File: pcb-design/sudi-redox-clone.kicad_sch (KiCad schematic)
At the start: 127 parts, among them J1 SIDE_CON, J2 0.91 OLED, J3 SWD_JLINK, J5 SIDE_CON, J8 BatCon, K1 KEYSW, K10 KEYSW, K11 KEYSW, K12 KEYSW, K13 KEYSW, K14 KEYSW, K15 KEYSW, K16 KEYSW, K17 KEYSW, K18 KEYSW, K2 KEYSW, K3 KEYSW, K4 KEYSW, K5 KEYSW, K6 KEYSW, K7 KEYSW, K8 KEYSW, K9 KEYSW, P1 USB_C_Plug_USB2.0, SW1 RST, U4 AMS1117-3.3, U5 CH340C, U6 TP4056, U7 nRF52832-QFxx, U8 MCP23017_SS, Y5 32MHz

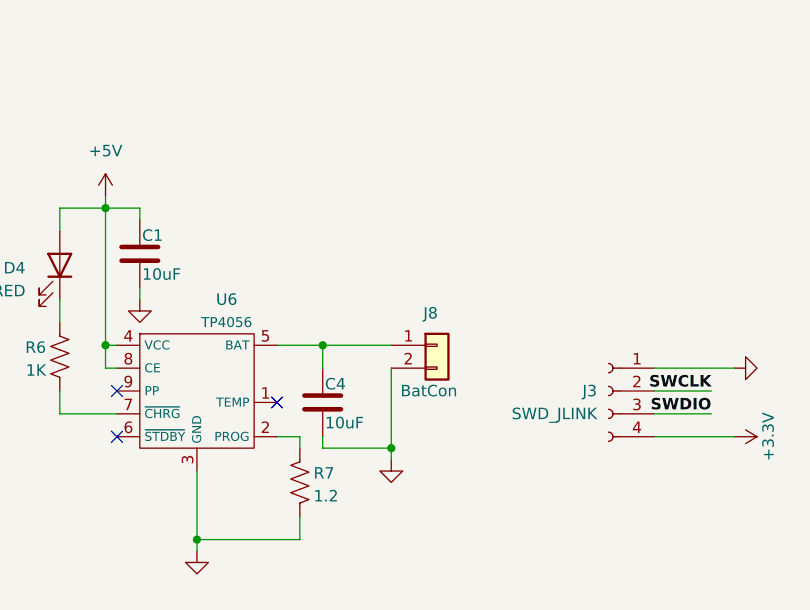
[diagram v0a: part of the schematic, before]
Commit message: [11-13-0459] add svg and switch to schematic
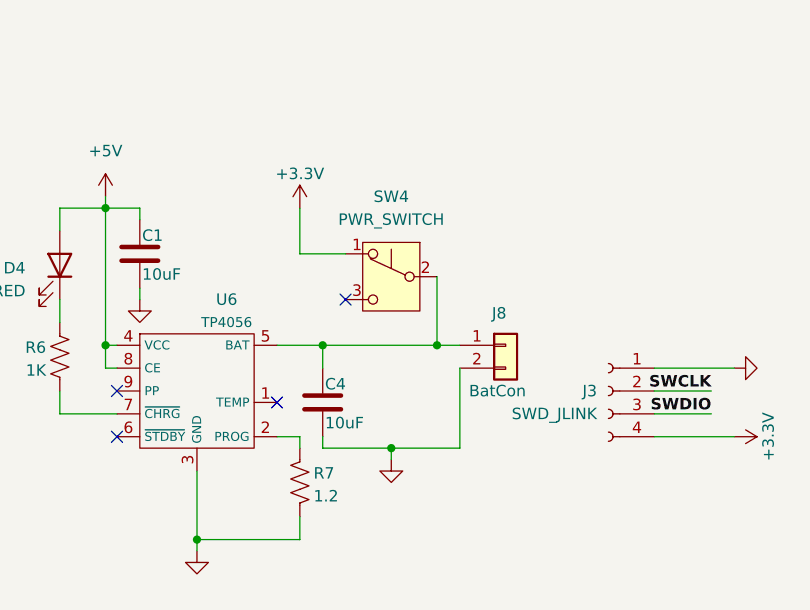
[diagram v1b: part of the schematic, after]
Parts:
- added SW4: PWR_SWITCH, Button_Switch_SMD:SW_SPDT_CK_JS102011SAQN, symbol Switch:SW_Push_SPDT
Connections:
- net +3.3V: now also SW4.1 (A)
- net at C4.1, J8.1 (Pin_1), U6.5 (BAT): now also SW4.2 (B)
- no-connect marks 28 -> 29
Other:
- moved on the sheet: J8
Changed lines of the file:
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@@
 	)
 	(junction
+		(at 177.8 49.53)
+		(diameter 0)
+		(color 0 0 0 0)
+	)
+	(junction
 		(at 330.2 182.88)
 		(diameter 0)
@@
 	)
 	(no_connect
+		(at 167.64 44.45)
+	)
+	(no_connect
 		(at 88.9 85.09)
 	)
@@
 	(wire
 		(pts
+			(xy 180.34 60.96) (xy 172.72 60.96)
+		)
+		(stroke
+			(width 0)
+			(type default)
+		)
+	)
+	(wire
+		(pts
 			(xy 247.65 101.6) (xy 250.19 101.6)
 		)
@@
 	(wire
 		(pts
-			(xy 172.72 52.07) (xy 172.72 60.96)
+			(xy 180.34 52.07) (xy 180.34 60.96)
 		)
 		(stroke
@@
 	(wire
 		(pts
+			(xy 167.64 39.37) (xy 162.56 39.37)
+		)
+		(stroke
+			(width 0)
+			(type default)
+		)
+	)
+	(wire
+		(pts
 			(xy 62.23 48.26) (xy 62.23 49.53)
 		)
@@
 	(wire
 		(pts
+			(xy 177.8 49.53) (xy 180.34 49.53)
+		)
+		(stroke
+			(width 0)
+			(type default)
+		)
+	)
+	(wire
+		(pts
 			(xy 228.6 161.29) (xy 231.14 161.29)
 		)
@@
 	(wire
 		(pts
-			(xy 165.1 49.53) (xy 172.72 49.53)
+			(xy 165.1 49.53) (xy 177.8 49.53)
 		)
 		(stroke
@@
 	(wire
 		(pts
+			(xy 162.56 39.37) (xy 162.56 34.29)
+		)
+		(stroke
+			(width 0)
+			(type default)
+		)
+	)
+	(wire
+		(pts
 			(xy 191.77 201.93) (xy 193.04 201.93)
 		)
@@
 	(wire
 		(pts
+			(xy 177.8 41.91) (xy 177.8 49.53)
+		)
+		(stroke
+			(width 0)
+			(type default)
+		)
+	)
+	(wire
+		(pts
 			(xy 278.13 26.67) (xy 278.13 30.48)
 		)
@@
 	)
 	(symbol
+		(lib_id "power:+3.3V")
+		(at 162.56 34.29 0)
+		(unit 1)
+		(exclude_from_sim no)
+		(in_bom yes)
+		(on_board yes)
+		(dnp no)
+		(fields_autoplaced yes)
+		(property "Reference" "#PWR035"
+			(at 162.56 38.1 0)
+			(effects
+				(font
+					(size 1.27 1.27)
+				)
+				(hide yes)
+			)
+		)
+		(property "Value" "+3.3V"
+			(at 162.56 30.48 0)
+			(effects
+				(font
+					(size 1.27 1.27)
+				)
+			)
+		)
+		(property "Footprint" ""
+			(at 162.56 34.29 0)
+			(effects
+				(font
+					(size 1.27 1.27)
+				)
+				(hide yes)
+			)
+		)
+		(property "Datasheet" ""
+			(at 162.56 34.29 0)
+			(effects
+				(font
+					(size 1.27 1.27)
+				)
+				(hide yes)
+			)
+		)
+		(property "Description" "Power symbol creates a global label with name \"+3.3V\""
+			(at 162.56 34.29 0)
+			(effects
+				(font
+					(size 1.27 1.27)
+				)
+				(hide yes)
+			)
+		)
+		(pin "1"
+		)
+		(instances
+			(project "sudi-redox-clone"
+				(path "/5bbd2338-13ff-49b0-9f87-5cbfec528c5b"
+					(reference "#PWR035")
+					(unit 1)
+				)
+			)
+		)
+	)
+	(symbol
 		(lib_id "Connector:TestPoint")
 		(at 119.38 152.4 270)
@@
 	(symbol
 		(lib_id "Connector_Generic:Conn_01x02")
-		(at 177.8 49.53 0)
+		(at 185.42 49.53 0)
 		(unit 1)
 		(exclude_from_sim no)
@@
 		(dnp no)
 		(property "Reference" "J8"
-			(at 176.276 45.974 0)
+			(at 183.896 45.974 0)
 			(effects
 				(font
@@
 		)
 		(property "Value" "BatCon"
-			(at 173.736 54.61 0)
+			(at 181.356 54.61 0)
 			(effects
 				(font
@@
 		)
 		(property "Footprint" "Connector_PinHeader_2.54mm:PinHeader_1x02_P2.54mm_Horizontal"
-			(at 177.8 49.53 0)
+			(at 185.42 49.53 0)
 			(effects
 				(font
@@
 		)
 		(property "Datasheet" "~"
-			(at 177.8 49.53 0)
+			(at 185.42 49.53 0)
 			(effects
 				(font
@@
 		)
 		(property "Description" "Generic connector, single row, 01x02, script generated (kicad-library-utils/schlib/autogen/connector/)"
-			(at 177.8 49.53 0)
+			(at 185.42 49.53 0)
 			(effects
 				(font
@@
 					(unit 1)
 				)
+			)
+		)
+	)
+	(symbol
+		(lib_id "Switch:SW_Push_SPDT")
+		(at 172.72 41.91 0)
+		(mirror y)
+		(unit 1)
+		(exclude_from_sim no)
+		(in_bom yes)
+		(on_board yes)
+		(dnp no)
+		(property "Reference" "SW4"
+			(at 172.72 33.02 0)
+			(effects
+				(font
+					(size 1.27 1.27)
+				)
+			)
+		)
+		(property "Value" "PWR_SWITCH"
+			(at 172.72 35.56 0)
+			(effects
+				(font
+					(size 1.27 1.27)
+				)
+			)
+		)
+		(property "Footprint" "Button_Switch_SMD:SW_SPDT_CK_JS102011SAQN"
+			(at 172.72 41.91 0)
+			(effects
+				(font
+					(size 1.27 1.27)
+				)
+				(hide yes)
+			)
+		)
+		(property "Datasheet" "~"
+			(at 172.72 41.91 0)
+			(effects
+				(font
+					(size 1.27 1.27)
+				)
+				(hide yes)
+			)
+		)
+		(property "Description" "Momentary Switch, single pole double throw"
+			(at 172.72 41.91 0)
+			(effects
+				(font
+					(size 1.27 1.27)
+				)
+				(hide yes)
+			)
+		)
+		(pin "3"
+		)
+		(pin "2"
+		)
+		(pin "1"
+		)
+		(instances
+			(project "sudi-redox-clone"
+				(path "/5bbd2338-13ff-49b0-9f87-5cbfec528c5b"
+					(reference "SW4")
+					(unit 1)
+				)

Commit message: [14-11-2129] init SUDI development board
nit
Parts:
- added U10: nRF52820-QDxx, Package_DFN_QFN:QFN-40-1EP_5x5mm_P0.4mm_EP3.6x3.6mm, symbol MCU_Nordic:nRF52820-QDxx
- added U9: nRF52833_QDxx, Package_DFN_QFN:QFN-40-1EP_5x5mm_P0.4mm_EP3.6x3.6mm, symbol MCU_Nordic:nRF52833_QDxx
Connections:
- new net: U10.37 (VSS), U10.41 (VSS)
- new net: U9.18 (VDD), U9.30 (VDD), U9.40 (VDD), U9.8 (VDD)
- new net: U9.37 (VSS), U9.41 (VSS)

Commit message: [16-11-1807] change chargin mechanism
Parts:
- removed AE3: 2.4GHz, RF_Antenna:Texas_SWRA117D_2.4GHz_Left, symbol Device:Antenna
- removed C3: 10uF/5V, Capacitor_SMD:C_0805_2012Metric_Pad1.18x1.45mm_HandSolder, symbol Device:C_Polarized
- removed C41: 0.8pF, Capacitor_SMD:C_0805_2012Metric_Pad1.18x1.45mm_HandSolder, symbol Device:C
- removed C42: 100nF, Capacitor_SMD:C_0805_2012Metric_Pad1.18x1.45mm_HandSolder, symbol Device:C
- removed D10, D11, D12, D16, D17, D18, D22, D23, D24, D28, D43, D44, D45, D46, D47, D48, D5, D6: WS2812B, CustomWS2185BFootPrint:LED_WS2812B_PLCC4_5.0x5.0mm_P3.2mm, symbol LED:WS2812B
- removed D13, D19, D25, D29, D30, D31, D8, D9: 1N5820, canadian_footprints:D_SOD123_axial-dual, symbol Diode:1N5820
- removed H8, H9: MountingHole_Pad, MountingHole:MountingHole_3.2mm_M3_DIN965_Pad, symbol Mechanical:MountingHole_Pad
- removed J8: BatCon, Connector_PinHeader_2.54mm:PinHeader_1x02_P2.54mm_Horizontal, symbol Connector_Generic:Conn_01x02
- removed L7: 3.9nH, Inductor_SMD:L_0603_1608Metric_Pad1.05x0.95mm_HandSolder, symbol Device:L
- removed U10: nRF52820-QDxx, Package_DFN_QFN:QFN-40-1EP_5x5mm_P0.4mm_EP3.6x3.6mm, symbol MCU_Nordic:nRF52820-QDxx
- removed U4: AMS1117-3.3, Package_TO_SOT_SMD:SOT-223-3_TabPin2, symbol Regulator_Linear:AMS1117-3.3
- removed U5: CH340C, Package_SO:SOIC-16_3.9x9.9mm_P1.27mm, symbol Interface_USB:CH340C
- removed U6: TP4056, Package_SO:SOIC-8-1EP_3.9x4.9mm_P1.27mm_EP2.29x3mm, symbol tp4056:TP4056
- removed U9: nRF52833_QDxx, Package_DFN_QFN:QFN-40-1EP_5x5mm_P0.4mm_EP3.6x3.6mm, symbol MCU_Nordic:nRF52833_QDxx
- removed Y5: 32MHz, Crystal:Crystal_SMD_2016-4Pin_2.0x1.6mm, symbol Device:Crystal_GND24
- added AE1: 2.4GHz, RF_Antenna:Texas_SWRA117D_2.4GHz_Left, symbol Device:Antenna
- added C11, C15: 0.1uF, Capacitor_SMD:C_0805_2012Metric_Pad1.18x1.45mm_HandSolder, symbol Device:C
- added C12, C13, C14, C16, C17: 10uF, Capacitor_SMD:C_0805_2012Metric_Pad1.18x1.45mm_HandSolder, symbol Device:C
- added C18: 12pF, Capacitor_SMD:C_0805_2012Metric_Pad1.18x1.45mm_HandSolder, symbol Device:C
- added C21: 0.8pF, Capacitor_SMD:C_0805_2012Metric_Pad1.18x1.45mm_HandSolder, symbol Device:C
- added C3: 4.7uF, Capacitor_SMD:C_0805_2012Metric_Pad1.18x1.45mm_HandSolder, symbol Device:C
- added D10, D11, D12, D13, D17, D18, D19, D23, D24, D25, D29, D30, D31, D36, D37, D38, D8, D9: WS2812B, LED_SMD:LED_WS2812B-2020_PLCC4_2.0x2.0mm, symbol LED:WS2812B-2020
- added D16, D22, D28, D33, D34, D35, D5, D6: 1N4148, canadian_footprints:D_SOD123_axial-dual, symbol Diode:1N5820
- added D32: red, LED_SMD:LED_0805_2012Metric_Pad1.15x1.40mm_HandSolder, symbol Device:LED
- added H1, H2: MountingHole_Pad, MountingHole:MountingHole_3.2mm_M3_DIN965_Pad, symbol Mechanical:MountingHole_Pad
- added J4: BatCon, Connector_PinHeader_2.54mm:PinHeader_1x02_P2.54mm_Horizontal, symbol Connector_Generic:Conn_01x02
- added JP1: END_TX, Jumper:SolderJumper-2_P1.3mm_Open_RoundedPad1.0x1.5mm, symbol Jumper:SolderJumper_2_Open
- added L1, L2: 22uH, Inductor_SMD:L_0603_1608Metric_Pad1.05x0.95mm_HandSolder, symbol Device:L
- added L3: 3.9nH, Inductor_SMD:L_0603_1608Metric_Pad1.05x0.95mm_HandSolder, symbol Device:L
- added Q1: PJA3404_(G1,D3,S2), Package_TO_SOT_SMD:SOT-23, symbol Simulation_SPICE:NMOS
- added Q2: PJA3405_(G1,D3,S2), Package_TO_SOT_SMD:SOT-23, symbol Simulation_SPICE:PMOS
- added R11: 1k, Resistor_SMD:R_0805_2012Metric_Pad1.20x1.40mm_HandSolder, symbol Device:R_US
- added R12, R5: 100k, Resistor_SMD:R_0805_2012Metric_Pad1.20x1.40mm_HandSolder, symbol Device:R_US
- added R13, R16: 100, Resistor_SMD:R_0805_2012Metric_Pad1.20x1.40mm_HandSolder, symbol Device:R_US
- added R14: 1.13k, Resistor_SMD:R_0805_2012Metric_Pad1.20x1.40mm_HandSolder, symbol Device:R_US
- added R15, R17: 1K, Resistor_SMD:R_0805_2012Metric_Pad1.20x1.40mm_HandSolder, symbol Device:R_US
- added SW3: PWR_SWITCH, Button_Switch_SMD:SW_SPDT_PCM12, symbol Switch:SW_Push_SPDT
- added U4: CH340C, Package_SO:SOIC-16_3.9x9.9mm_P1.27mm, symbol Interface_USB:CH340C
- added U5: BQ24075RGT_DPPM, Package_DFN_QFN:VQFN-16-1EP_3x3mm_P0.5mm_EP1.6x1.6mm, symbol Battery_Management:BQ24075RGT
- added U6: TPS63002_SEPIC_5V, Package_SON:Texas_DRC0010J_ThermalVias, symbol Regulator_Switching:TPS63002
- added U9: TPS63001_SEPIC_3V3, Package_SON:Texas_DRC0010J_ThermalVias, symbol Regulator_Switching:TPS63001
- added Y1: 32MHz_CF4032M00020001, Crystal:Crystal_SMD_2016-4Pin_2.0x1.6mm, symbol Device:Crystal_GND24
- C1: value 10uF -> 4.7uF
- C19: value 12pF -> 100nF
- C36: value 100nF -> 100nF/NC
- C40: value 100nF/NC -> 100nF
- D1, D14, D15, D2, D20, D21, D26, D27, D3, D7: value 1N5820 -> 1N4148
- D4: value RED -> green
- J2: value 0.91 OLED -> SWD_JLINK; footprint Connector_PinHeader_2.54mm:PinHeader_1x04_P2.54mm_Vertical -> Connector_PinHeader_2.54mm:PinHeader_1x04_P2.54mm_Horizontal
- J3: value SWD_JLINK -> 0.91 OLED; footprint Connector_PinHeader_2.54mm:PinHeader_1x04_P2.54mm_Horizontal -> Connector_PinHeader_2.54mm:PinHeader_1x04_P2.54mm_Vertical
- R6: value 1K -> 46.4K
- R7: value 1.2 -> 1.18k
- SW4: value PWR_SWITCH -> 5V_EN; footprint Button_Switch_SMD:SW_SPDT_CK_JS102011SAQN -> Button_Switch_SMD:SW_SPDT_PCM12
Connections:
- net +3.3V: now also C38.1, C39.1, C40.1, J1.B9 (CC1), J2.4 (Pin_4), J3.2 (Pin_2), J5.B9 (CC1), C16.1, C17.1, U4.16 (VCC), U4.4 (V3), U9.1 (VOUT), U9.10 (FB); no longer C20.1, C35.1, C36.1, J3.4 (Pin_4), SW4.1 (A)
- net +5V: now also C12.1, C13.1, D10.4 (VDD), D11.4 (VDD), D12.4 (VDD), D13.4 (VDD), D17.4 (VDD), D18.4 (VDD), D19.4 (VDD), D23.4 (VDD), D24.4 (VDD), D25.4 (VDD), D29.4 (VDD), D30.4 (VDD), D31.4 (VDD), D36.4 (VDD), D37.4 (VDD), D38.4 (VDD), D8.4 (VDD), D9.4 (VDD), U6.1 (VOUT), U6.10 (FB); no longer C1.1, C2.1, D4.2 (A), FB1.2
- net GND: now also C19.2, C20.1, C35.1, C36.1, C38.2, C39.2, C40.2, R6.2, R7.2, SW4.3 (C), C11.2, C12.2, C13.2, C14.2, C15.2, C16.2, C17.2, C18.1, C21.2, C3.2, D10.2 (VSS), D11.2 (VSS), D12.2 (VSS), D13.2 (VSS), D17.2 (VSS), D18.2 (VSS), D19.2 (VSS), D23.2 (VSS), D24.2 (VSS), D25.2 (VSS), D29.2 (VSS), D30.2 (VSS), D31.2 (VSS), D36.2 (VSS), D37.2 (VSS), D38.2 (VSS), D8.2 (VSS), D9.2 (VSS), J4.1 (Pin_1), Q1.2 (S), Q2.1 (G), R14.2, R5.2, SW3.3 (C), U4.1 (GND), U5.17 (VSS), U5.4 (~{CE}), U5.6 (EN1), U5.8 (VSS), U6.11 (PGND), U6.3 (PGND), U6.9 (GND), U9.11 (PGND), U9.3 (PGND), U9.9 (GND), Y1.2, Y1.4; no longer C19.1, C20.2, C35.2, C36.2, C38.1, C39.1, C40.1, R7.1
- net P0.00/XL1: now also TP1.1; no longer TP13.1
- net P0.01/XL2: now also TP2.1; no longer TP14.1
- net P0.02/AIN0: now also TP3.1; no longer TP15.1
- net P0.03/AIN1: now also TP4.1; no longer TP16.1
- net P0.04/AIN2: now also TP5.1; no longer TP17.1
- net P0.05/AIN3: now also TP6.1; no longer TP18.1
- net P0.19: now also TP7.1; no longer TP1.1
- net P0.20: now also TP8.1; no longer TP3.1
- net P0.22: now also TP9.1; no longer TP2.1
- net P0.23: now also TP10.1; no longer TP4.1
- net P0.24: now also TP11.1; no longer TP5.1
- net P0.25: now also TP12.1; no longer TP6.1
- net P0.26: now also TP13.1; no longer TP7.1
- net P0.27: now also TP14.1; no longer TP8.1
- net P0.28/AIN4: now also TP15.1; no longer TP9.1
- net P0.29/AIN5: now also TP16.1; no longer TP10.1
- net P0.30/AIN6: now also TP17.1; no longer TP11.1
- net P0.31/AIN7: now also TP18.1; no longer TP12.1
- net RX: now also U4.2 (TXD)
- net SCL: now also J3.3 (Pin_3); no longer J2.3 (Pin_3)
- net SDA: now also J3.4 (Pin_4); no longer J2.4 (Pin_4)
- net SWCLK: now also J2.2 (Pin_2); no longer J3.2 (Pin_2)
- net SWDIO: now also J2.3 (Pin_3); no longer J3.3 (Pin_3)
- net TX: now also D8.3 (DIN), JP1.2 (B), U4.3 (RXD)
- net row1: now also D14.1 (K), D20.1 (K), D26.1 (K), D33.1 (K), D5.1 (K); no longer D7.1 (K)
- net row2: now also D15.1 (K), D21.1 (K), D27.1 (K), D34.1 (K), D6.1 (K); no longer D14.1 (K), D20.1 (K), D26.1 (K)
- net row3: now also D7.1 (K), D16.1 (K), D22.1 (K), D28.1 (K), D35.1 (K); no longer D15.1 (K), D21.1 (K), D27.1 (K)
- net at K17.2: now also D34.2 (A)
- net at K13.2: now also D26.2 (A)
- net at K7.2: now also D14.2 (A)
- net at C8.2, U7.34 (XC1): now also Y1.3
- net at K6.2: now also D7.2 (A)
- net at K10.2: now also D20.2 (A)
- net at K4.2: now also D5.2 (A); no longer D7.2 (A)
- net at P1.A4 (VBUS), P1.A9 (VBUS), P1.B4 (VBUS)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: now also Q2.3 (D); no longer FB1.1
- net at P1.A6 (D+): now also U4.5 (UD+)
- net at P1.A7 (D-): now also U4.6 (UD-)
- net at K8.2: now also D15.2 (A); no longer D14.2 (A)
- net at K16.2: now also D33.2 (A)
- net at SW1.2, U7.24 (P0.21/~{RESET}): now also C19.1
- net at U7.33 (DEC3): now also C36.2; no longer C40.2
- net at U7.30 (ANT): now also C21.1, L3.2
- net at K11.2: now also D21.2 (A); no longer D20.2 (A)
- net at K15.2: now also D28.2 (A); no longer D27.2 (A)
- net at K14.2: now also D27.2 (A); no longer D26.2 (A)
- net at K12.2: now also D22.2 (A); no longer D21.2 (A)
- net at K9.2: now also D16.2 (A); no longer D15.2 (A)
- net at K5.2: now also D6.2 (A)
- net at U7.1 (DEC1): now also C20.2; no longer C38.2
- net at U7.32 (DEC2): now also C35.2; no longer C39.2
- net at U7.35 (XC2): now also C18.2, Y1.1; no longer C19.2
- net at K18.2: now also D35.2 (A)
- net at SW4.2 (B): now also U6.6 (EN); no longer C4.1
- net TMR: now reaches R6.1
- net TMR: now also U5.14 (TMR)
- net at D4.1 (K): now also U5.7 (~{PGOOD}); no longer R6.2
- removed net +3V7: J1.B9 (CC1), J2.2 (Pin_2), J5.B9 (CC1)
- net Tx renamed END_TX
- net END_TX: now also D38.1 (DOUT), JP1.1 (A)
- new net: D32.1 (K), U5.9 (~{CHG})
- new net: R12.2, SW3.1 (A)
- new net: AE1.1 (A), L3.1
- new net: D4.2 (A), R15.1
- new net: C15.1, R16.2, U9.6 (EN), U9.7 (PS/SYNC), U9.8 (VINA)
- new net: D13.1 (DOUT), D19.3 (DIN)
- new net: D10.1 (DOUT), D13.3 (DIN)
- new net: C11.1, R13.2, SW4.1 (A), U6.7 (PS/SYNC), U6.8 (VINA)
- new net: D30.1 (DOUT), D37.3 (DIN)
- new net: L2.1, U9.2 (L2)
- new net: L2.2, U9.4 (L1)
- new net: FB1.1, Q2.2 (S)
- new net: D25.1 (DOUT), D31.3 (DIN)
- new net: D19.1 (DOUT), D25.3 (DIN)
- new net: D12.1 (DOUT), D18.3 (DIN)
- new net: D12.3 (DIN), D9.1 (DOUT)
- new net: D29.1 (DOUT), D36.3 (DIN)
- new net: D23.1 (DOUT), D29.3 (DIN)
- new net: L1.1, U6.2 (L2)
- new net: L1.2, U6.4 (L1)
- new net: Q1.1 (G), R11.2
- new net: D31.1 (DOUT), D38.3 (DIN)
- new net: D17.1 (DOUT), D23.3 (DIN)
- new net: D11.1 (DOUT), D17.3 (DIN)
- new net: D11.3 (DIN), D8.1 (DOUT)
- new net: D24.1 (DOUT), D30.3 (DIN)
- new net: D18.1 (DOUT), D24.3 (DIN)
- new net: D32.2 (A), R17.1
- new net +BATT: C1.1, J4.2 (Pin_2), R12.1, U5.2 (BAT), U5.3 (BAT)
- new net DOUT1: D36.1 (DOUT), D9.3 (DIN)
- new net DOUT2: D10.3 (DIN), D37.1 (DOUT)
- new net ILIM: R7.1, U5.12 (ILIM)
- new net ISET: R14.1, U5.16 (ISET)
- new net SYSOFF: Q1.3 (D), SW3.2 (B), U5.15 (SYSOFF)
- new net VBUS: C2.1, FB1.2, R11.1, R5.1, U5.13 (IN)
- new net VDD: C14.1, C3.1, C4.1, R13.1, R15.2, R16.1, R17.2, U5.10 (OUT), U5.11 (OUT), U5.5 (EN2), U6.5 (VIN), U9.5 (VIN)
- no-connect marks 29 -> 25
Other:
- note added: "CONNECTOR"
- note added: "DPPM"
- note added: "EN 6 IN Enable input (1 enabled, 0 disabled)"
- note added: "PWR SWITCH"
- note added: "Program Fast-Charge Safety Timer (TMR): RTMR = tMAXCHG / (10 × KTMR ) KTMR = 48 s/kΩ from the electrical characteristics table. RTMR = (6.25 hr × 3600 s/hr) / (10 × 48 s/kΩ) = 46.8 kΩ -> 46.4 kΩ"
- note added: "Program the Fast Charge Current (ISET): RISET = KISET / ICHG KISET = 890 AΩ from the electrical characteristics table. RISET = 890 AΩ / 0.8 A = 1.1125 kΩ -> 1.13 kΩ"
- note added: "Program the Input Current Limit (ILIM) RILIM = KILIM / II_MAX KILIM = 1550 AΩ from the electrical characteristics table. RISET = 1550 AΩ / 1.3 A = 1.192 kΩ -> 1.18 kΩ"
- note added: "SEPIC 3.3V"
- note added: "SEPIC 5V"
- note added: "SYSOFF High = Enable Low = disable System Enable Input. Connect SYSOFF high to turn off the FET connecting the battery to the system output."
- note removed: "ADD USB C Backup with usb serial converter"
- note removed: "NOTE: Used Real Diode 1N4148"
- note removed: "OLED 0.91'"
- note removed: "TODO: ADD USB serial interface or use NRF52833/NRF52830 with built in usb feature"

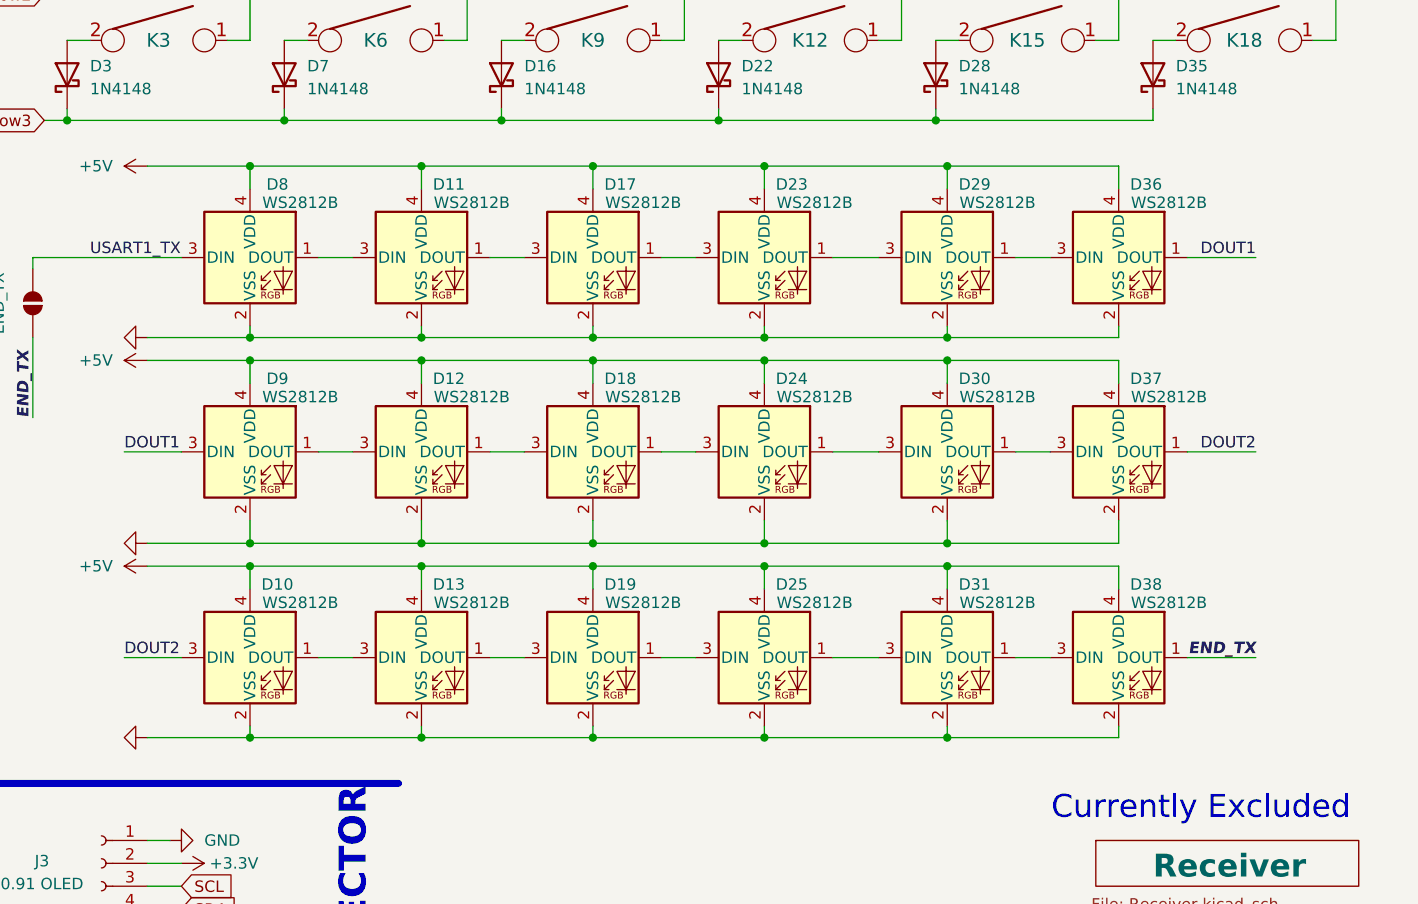
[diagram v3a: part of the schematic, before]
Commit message: [16-11-1807] add capacitor to WS2812C-2020
change gif
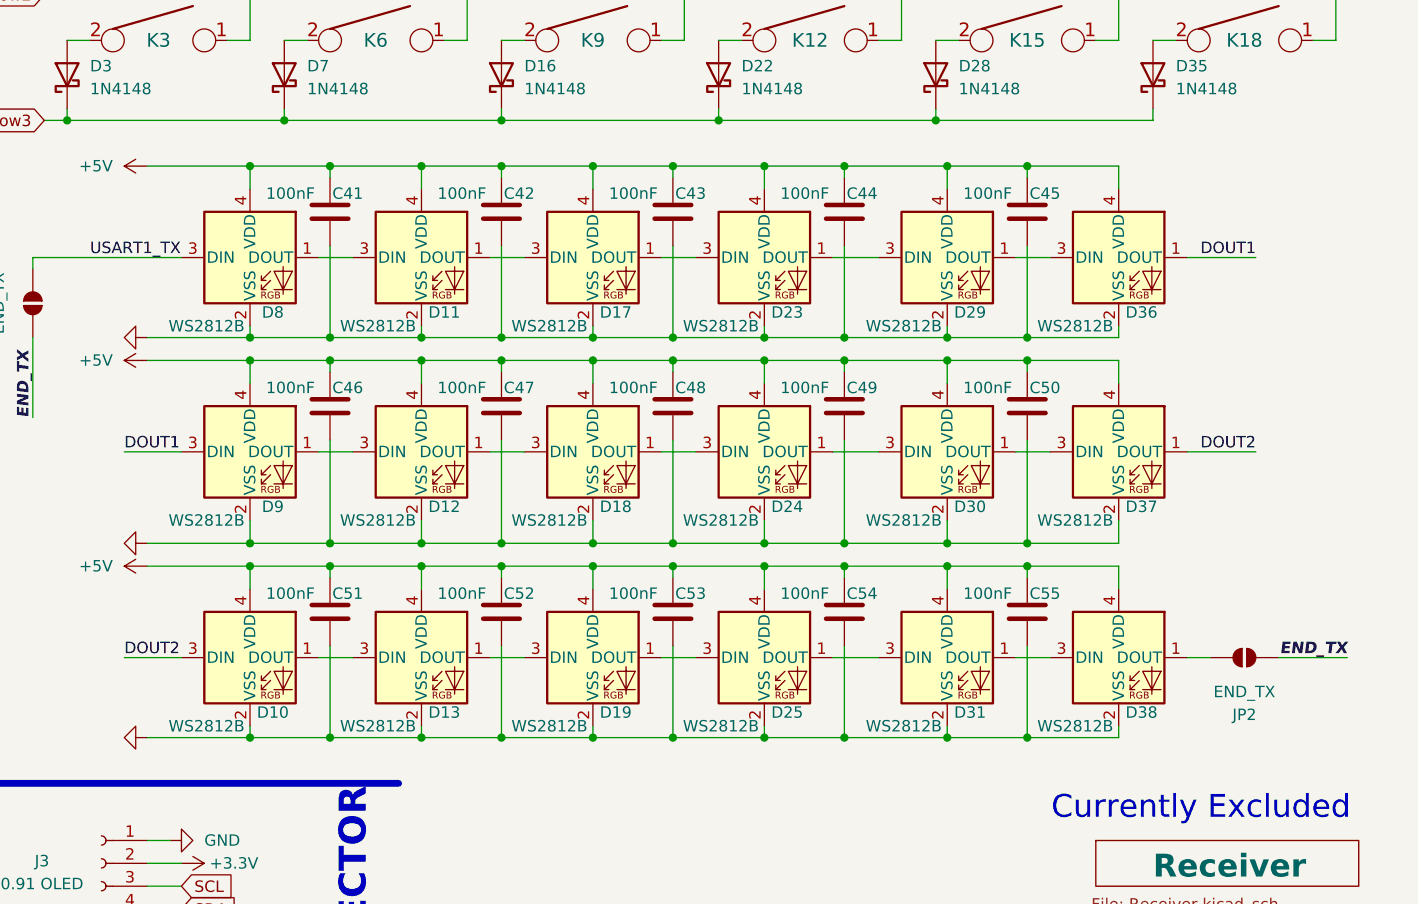
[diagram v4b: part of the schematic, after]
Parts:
- added C41, C42, C43, C44, C45, C46, C47, C48, C49, C50, C51, C52, C53, C54, C55: 100nF, Capacitor_SMD:C_0805_2012Metric_Pad1.18x1.45mm_HandSolder, symbol Device:C
- added JP2: END_TX, Jumper:SolderJumper-2_P1.3mm_Open_RoundedPad1.0x1.5mm, symbol Jumper:SolderJumper_2_Open
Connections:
- net +5V: now also C41.1, C42.1, C43.1, C44.1, C45.1, C46.1, C47.1, C48.1, C49.1, C50.1, C51.1, C52.1, C53.1, C54.1, C55.1
- net END_TX: now also JP2.1 (A); no longer D38.1 (DOUT)
- net GND: now also C41.2, C42.2, C43.2, C44.2, C45.2, C46.2, C47.2, C48.2, C49.2, C50.2, C51.2, C52.2, C53.2, C54.2, C55.2
- new net: D38.1 (DOUT), JP2.2 (B)

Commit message: [17-11-1825] tweak values and silkscreen
nit, add pdf

nit

nit schematic

add svg
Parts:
- added C56: 0.1uF, Capacitor_SMD:C_0805_2012Metric_Pad1.18x1.45mm_HandSolder, symbol Device:C
- added U10: MAX17048, Package_DFN_QFN:DFN-8-1EP_2x2mm_P0.5mm_EP0.8x1.6mm, symbol PCM_marbastlib-various:MAX17048
- TP1: value TestPoint -> 0
- TP10: value TestPoint -> 23
- TP11: value TestPoint -> 24
- TP12: value TestPoint -> 25
- TP13: value TestPoint -> 26
- TP14: value TestPoint -> 27
- TP15: value TestPoint -> 28
- TP16: value TestPoint -> 29
- TP17: value TestPoint -> 30
- TP18: value TestPoint -> 31
- TP2: value TestPoint -> 1
- TP3: value TestPoint -> 2
- TP4: value TestPoint -> 3
- TP5: value TestPoint -> 4
- TP6: value TestPoint -> 5
- TP7: value TestPoint -> 19
- TP8: value TestPoint -> 20
- TP9: value TestPoint -> 22
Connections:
- net +3.3V: now also C56.1, U10.2 (CELL), U10.3 (VDD)
- net GND: now also C56.2, U10.1 (CTG), U10.4 (GND), U10.6 (QSTRT), U10.9 (GND)
- net SCL: now also U10.7 (SCL)
- net SDA: now also U10.8 (SDA)
- no-connect marks 25 -> 26
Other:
- moved on the sheet: AE1, C14, C15, C16, C17, C18, C19, C20, C21, C35, C36, C37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
